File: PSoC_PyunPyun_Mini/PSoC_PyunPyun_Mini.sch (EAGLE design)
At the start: 33 parts, among them IC1 LM358N, IC2 LM358N

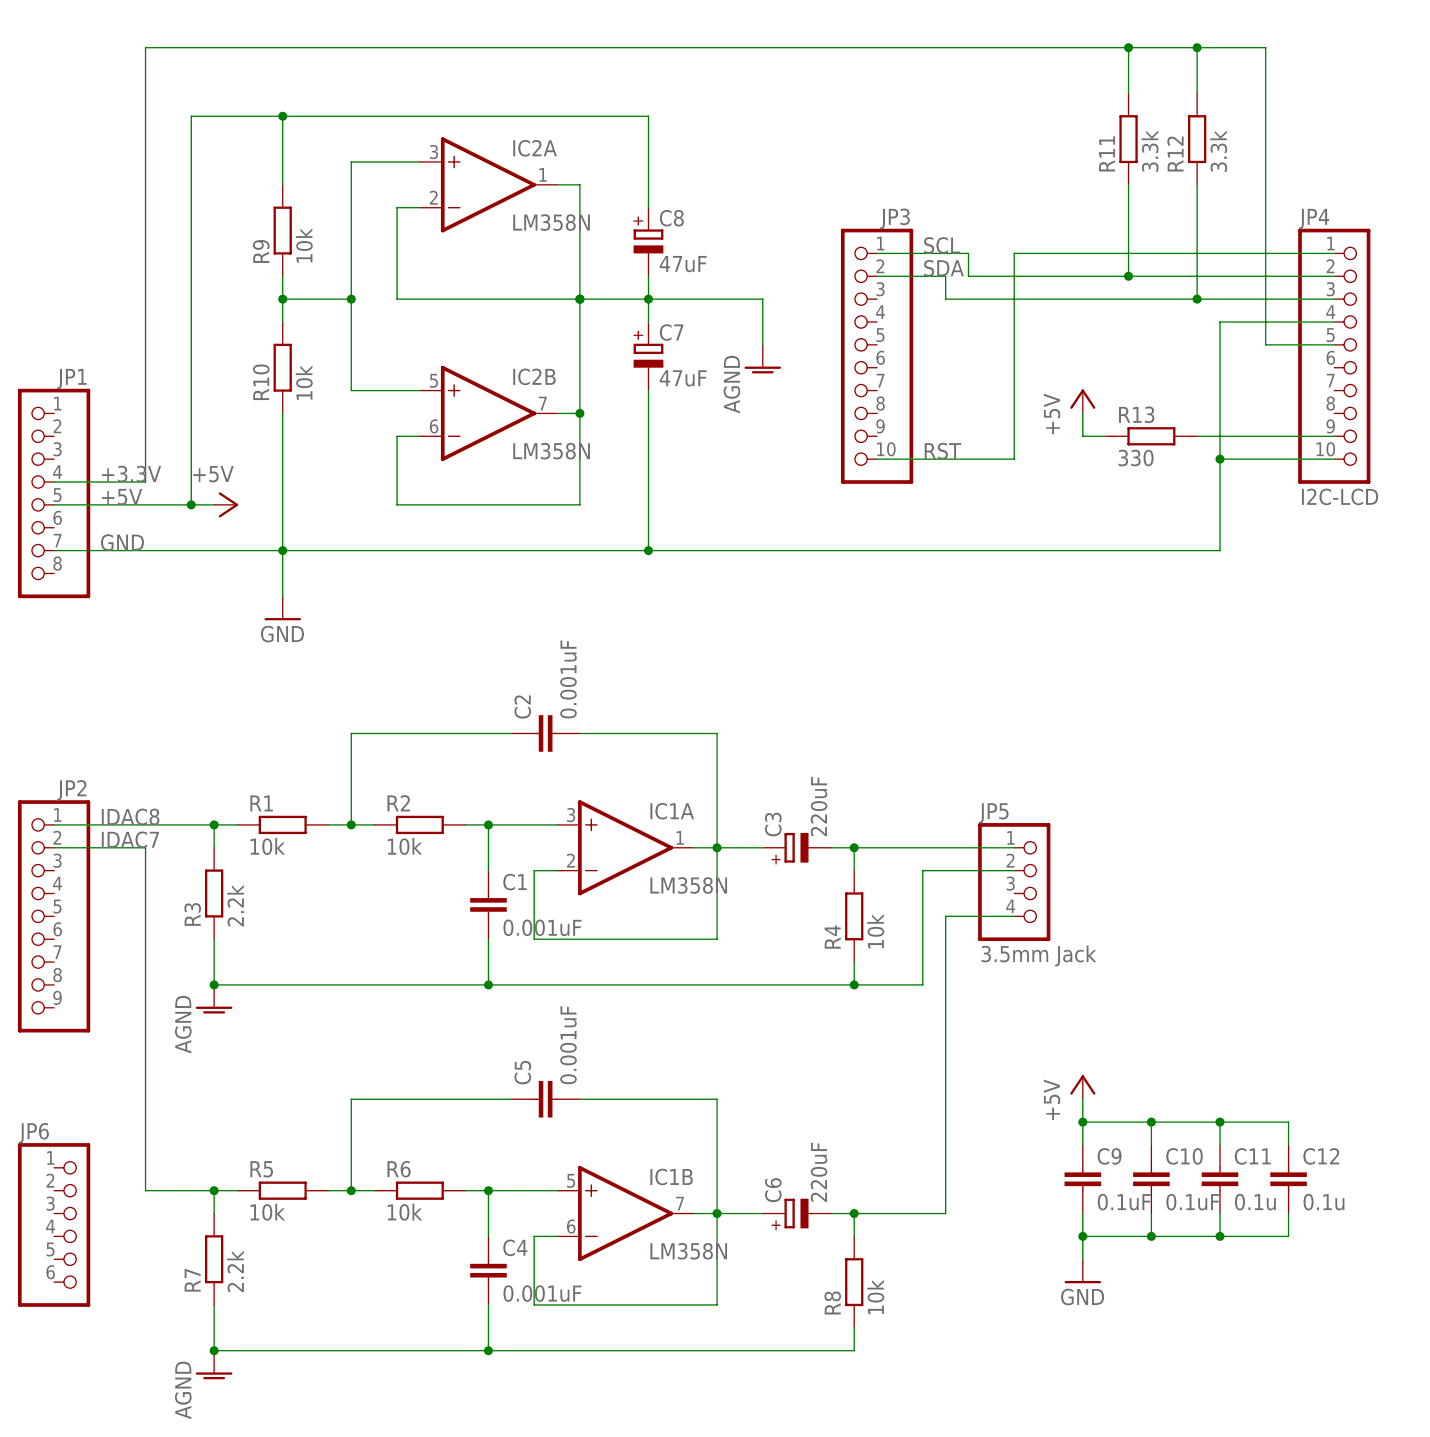
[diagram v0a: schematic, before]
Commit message: PSoC Pyun Pyun miniの基板図を作成
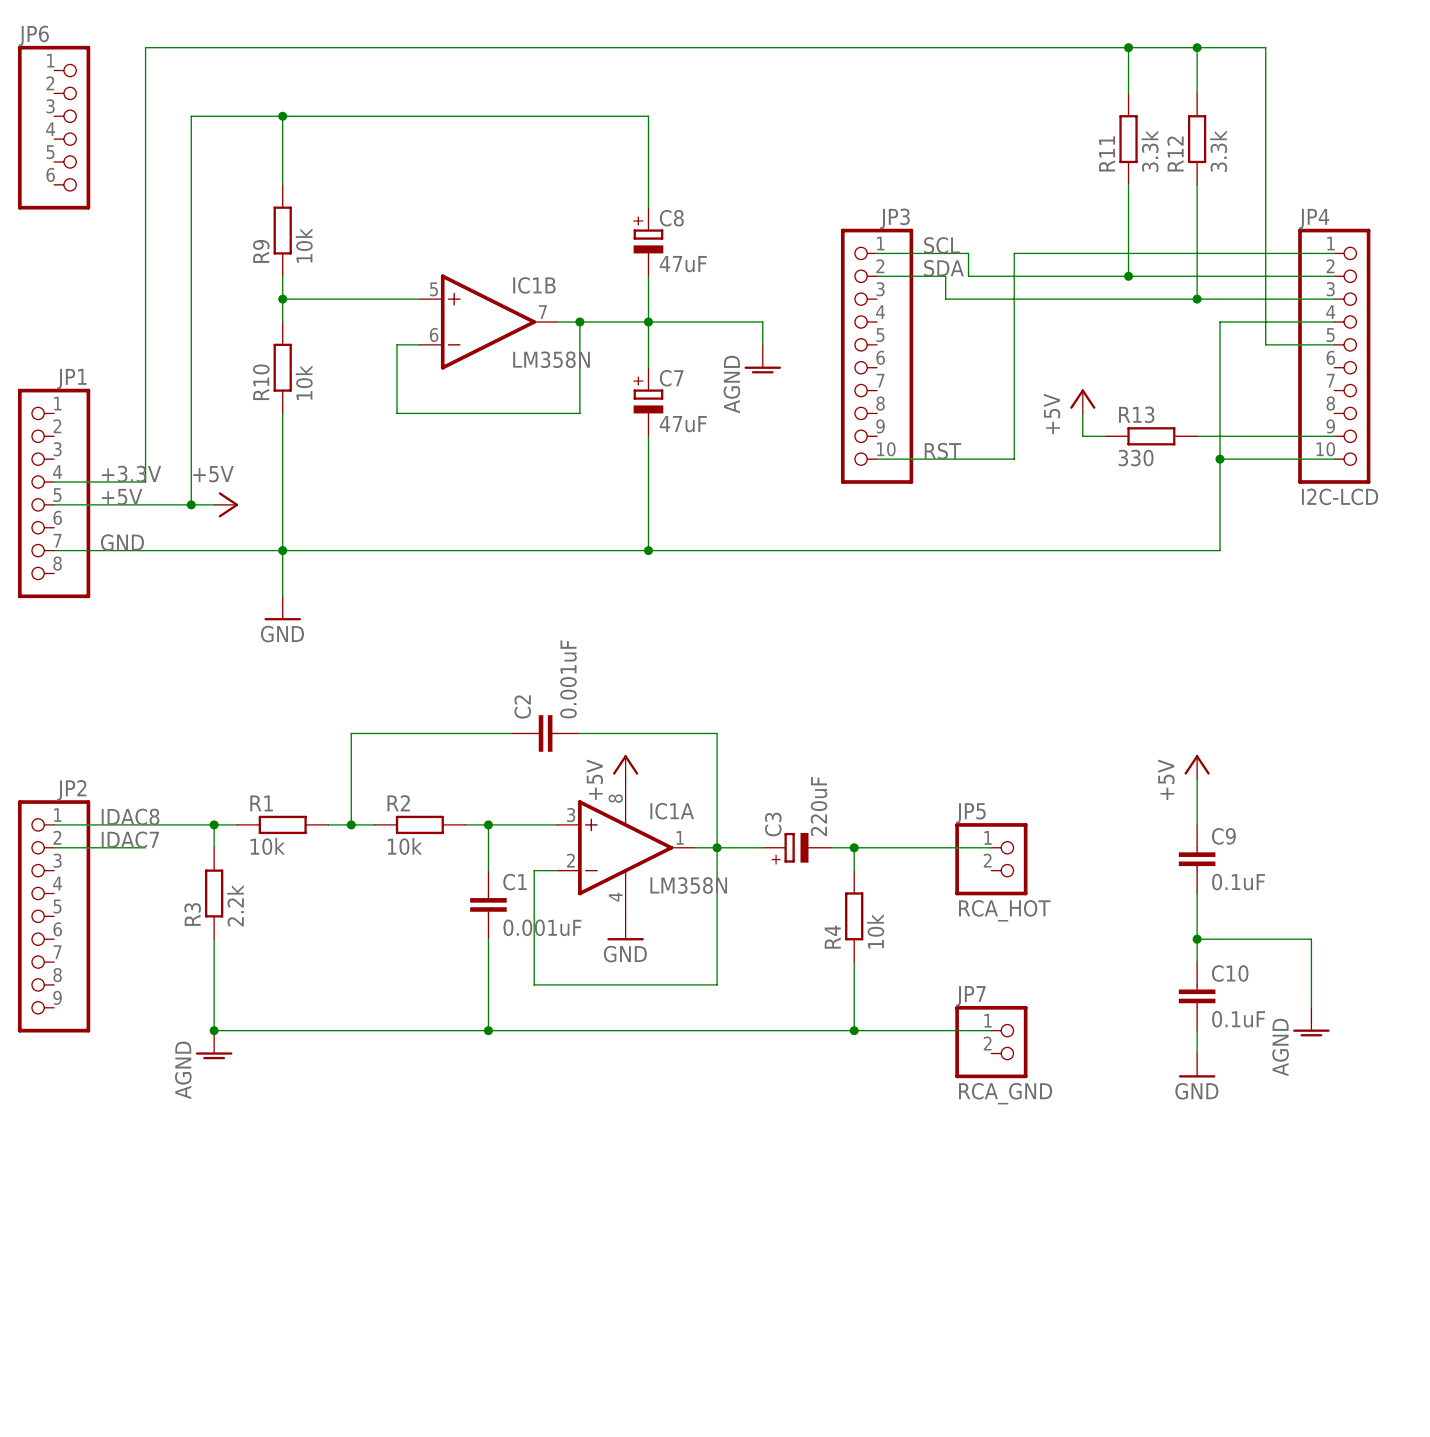
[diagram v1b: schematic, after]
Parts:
- removed C11, C12: 0.1u, rcl:C-EU050-024X044
- removed C4, C5: 0.001uF, rcl:C-EU050-024X044
- removed C6: 220uF, rcl:CPOL-EUE5-8.5
- removed IC2: LM358N, linear:LM358N
- removed R5, R6, R8: 10k, rcl:R-EU_0207/7
- removed R7: 2.2k, rcl:R-EU_0207/7
- added JP7: RCA_GND, pinhead:PINHD-1X2
- JP5: value 3.5mm Jack -> RCA_HOT; device pinhead:PINHD-1X4 -> pinhead:PINHD-1X2
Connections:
- removed net N$11: C4.1, IC1B.+IN, R6.2
- removed net N$12: C5.2, C6.+, IC1B.-IN, IC1B.OUT
- removed net N$14: C6.-, JP5.4, R8.2
- removed net N$9: C5.1, R5.2, R6.1
- net +5V: now also IC1P.V+; no longer C10.1, C11.1, C12.1
- net AGND: now also C10.1, C9.2, IC1B.-IN, IC1B.OUT, JP7.1; no longer C4.2, IC2A.-IN, IC2A.OUT, IC2B.-IN, IC2B.OUT, JP5.2, R7.1, R8.1
- net GND: now also IC1P.V-; no longer C11.2, C12.2, C9.2
- net IDAC7: no longer R5.1, R7.2
- net N$8: now also IC1B.+IN; no longer IC2A.+IN, IC2B.+IN
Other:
- moved on the sheet: C10, C7, C9, IC1B, JP6
